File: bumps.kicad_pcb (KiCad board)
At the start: 2 copper layers, 111.1 x 65.4 mm, 126 parts, among them M1 CONN_1, M2 CONN_1, M3 CONN_1, P1 Micro-E, P10 Mot-A, P11 Mot-A, P12 Mot-X, P13 T1, P14 T2, P15 T3, P16 MPower, P17 PWM-2, P18 PWM-1, P19 END-X, P2 DIL6, P20 END-Y, P21 END-Z, P22 Mot-X, P23 Mot-Y, P24 Mot-Y, P25 Mot-Z, P26 Mot-Z, P27 Aux, P29 PWM, P3 Mot-E, P4 Mot-E, P5 DIL6, P6 DIL6, P7 DIL6, P8 P8 Header, P9 P9 Header, Q1 N-FET, Q2 N-FET, Q3 FDS9926A, Q4 FDS9926A, U1 E-Polo, U2 A-Polo, U3 X-Polo, U4 Y-Polo, U5 Z-Polo, U6 MC34063, U7 AP1117/3.3

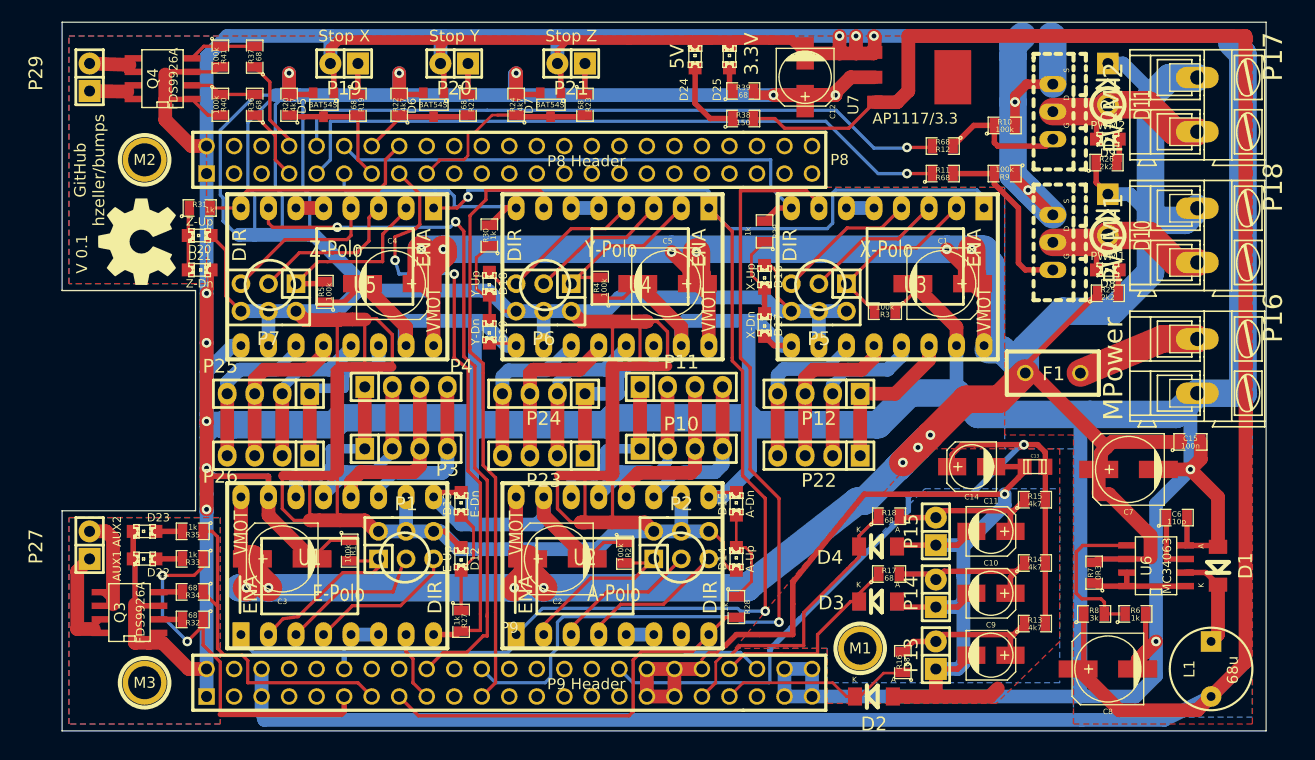
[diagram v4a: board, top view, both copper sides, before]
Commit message: o Some updates of labels.
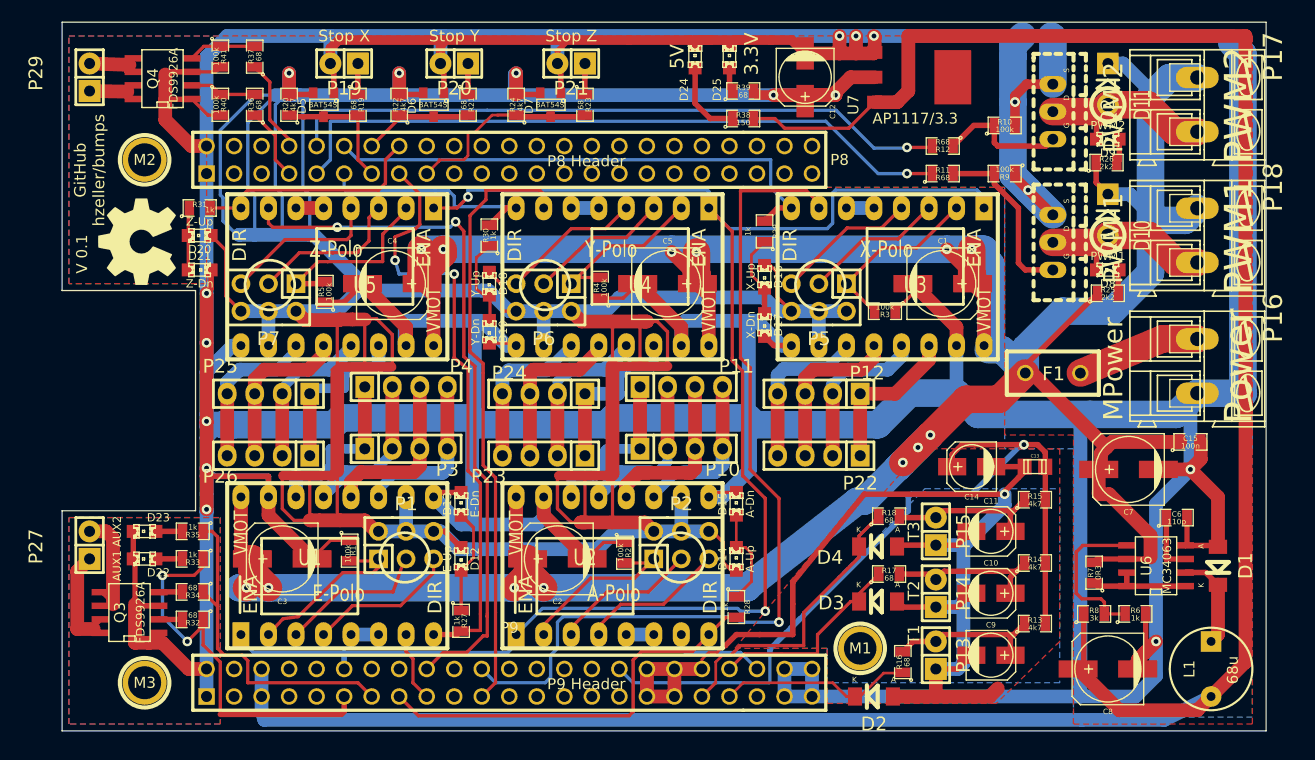
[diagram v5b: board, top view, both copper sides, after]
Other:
- board text added: "PWM1"
- board text added: "PWM2"
- board text added: "T1"
- board text added: "T2"
- board text added: "T3"
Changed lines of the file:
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@@
     (area 42.961076 19.039999 162.316583 94.234)
     (thickness 1.6)
-    (drawings 24)
+    (drawings 30)
     (tracks 1313)
     (zones 0)
@@
     (pad_to_mask_clearance 0)
     (aux_axis_origin 0 0)
-    (visible_elements FFFFFF7F)
+    (visible_elements FFFFEF7F)
     (pcbplotparams
       (layerselection 270565377)
@@
     (descr "1 pin")
     (tags "CONN DEV")
-    (fp_text reference P13 (at 0 -2.286 90) (layer F.SilkS)
+    (fp_text reference P13 (at 0 2.54 90) (layer F.SilkS)
       (effects (font (size 1.27 1.27) (thickness 0.2032)))
     )
@@
     (descr "1 pin")
     (tags "CONN DEV")
-    (fp_text reference P14 (at 0 -2.286 90) (layer F.SilkS)
+    (fp_text reference P14 (at 0 2.54 90) (layer F.SilkS)
       (effects (font (size 1.27 1.27) (thickness 0.2032)))
     )
@@
     (descr "1 pin")
     (tags "CONN DEV")
-    (fp_text reference P15 (at 0 -2.286 90) (layer F.SilkS)
+    (fp_text reference P15 (at 0 2.54 90) (layer F.SilkS)
       (effects (font (size 1.27 1.27) (thickness 0.2032)))
     )
@@
     (descr "1 pin")
     (tags "CONN DEV")
-    (fp_text reference P22 (at 0 -2.286 180) (layer F.SilkS)
+    (fp_text reference P22 (at -3.81 -2.54 180) (layer F.SilkS)
       (effects (font (size 1.27 1.27) (thickness 0.2032)))
     )
@@
     (descr "1 pin")
     (tags "CONN DEV")
-    (fp_text reference P23 (at 0 -2.286 180) (layer F.SilkS)
+    (fp_text reference P23 (at 5.08 -1.905 180) (layer F.SilkS)
       (effects (font (size 1.27 1.27) (thickness 0.2032)))
     )
@@
     (descr "1 pin")
     (tags "CONN DEV")
-    (fp_text reference P24 (at 0 -2.286 180) (layer F.SilkS)
+    (fp_text reference P24 (at 3.175 1.905 180) (layer F.SilkS)
       (effects (font (size 1.27 1.27) (thickness 0.2032)))
     )
@@
     (descr "1 pin")
     (tags "CONN DEV")
-    (fp_text reference P10 (at 0 -2.286) (layer F.SilkS)
+    (fp_text reference P10 (at 3.81 1.905) (layer F.SilkS)
       (effects (font (size 1.27 1.27) (thickness 0.2032)))
     )
@@
     (descr "1 pin")
     (tags "CONN DEV")
-    (fp_text reference P11 (at 0 -2.286) (layer F.SilkS)
+    (fp_text reference P11 (at 5.08 -1.905) (layer F.SilkS)
       (effects (font (size 1.27 1.27) (thickness 0.2032)))
     )
@@
     (descr "1 pin")
     (tags "CONN DEV")
-    (fp_text reference P12 (at 0 -2.286 180) (layer F.SilkS)
+    (fp_text reference P12 (at -4.445 1.905 180) (layer F.SilkS)
       (effects (font (size 1.27 1.27) (thickness 0.2032)))
     )
@@
       (xy -2.42316 3.59156)) (layer F.SilkS) (width 0.00254))
   )
+  (gr_text PWM2 (at 156.21 35.56 90) (layer F.SilkS)
+    (effects (font (size 2.54 2.54) (thickness 0.508)))
+  )
+  (gr_text PWM1 (at 156.21 47.625 90) (layer F.SilkS)
+    (effects (font (size 2.54 2.54) (thickness 0.508)))
+  )
+  (gr_text Power (at 156.21 59.69 90) (layer F.SilkS)
+    (effects (font (size 2.54 2.54) (thickness 0.508)))
+  )
+  (gr_text T2 (at 126.238 80.391 90) (layer F.SilkS)
+    (effects (font (size 1.0668 1.0668) (thickness 0.2032)))
+  )
+  (gr_text T1 (at 126.238 84.455 90) (layer F.SilkS)
+    (effects (font (size 1.0668 1.0668) (thickness 0.2032)))
+  )
+  (gr_text T3 (at 126.238 74.93 90) (layer F.SilkS)
+    (effects (font (size 1.0668 1.0668) (thickness 0.2032)))
+  )
   (gr_text "Stop Z" (at 94.615 29.21) (layer F.SilkS)

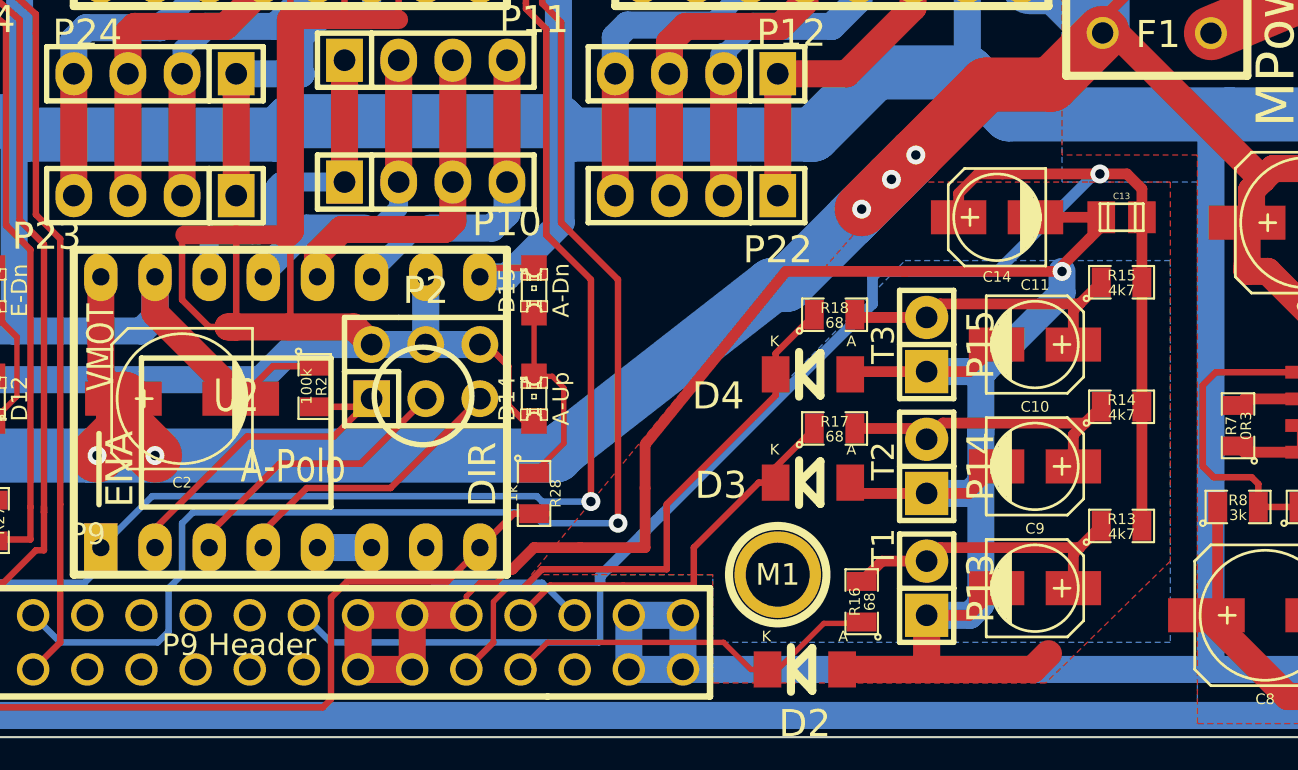
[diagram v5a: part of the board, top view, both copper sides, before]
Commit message: o Straighten out motor power trace to lower part a bit.
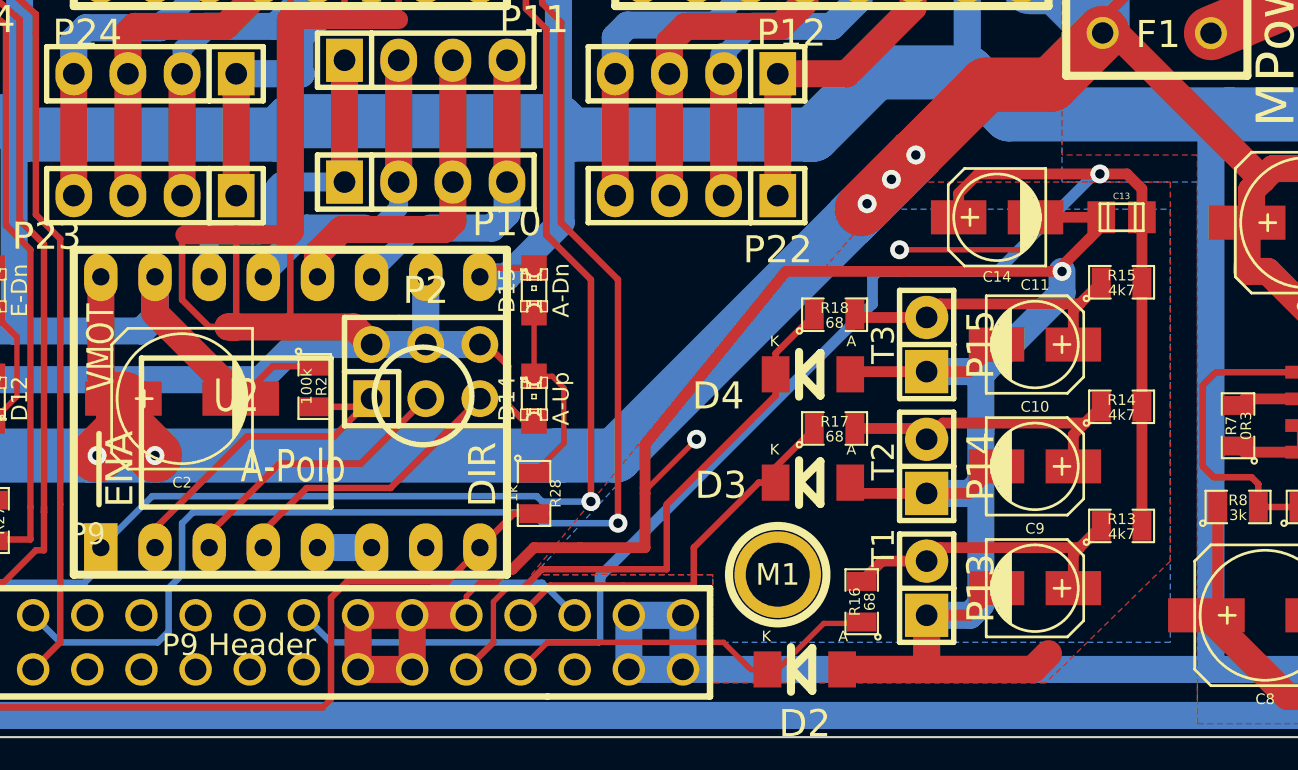
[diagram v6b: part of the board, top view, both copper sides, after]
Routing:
- net AGND: track 114.8 -> 125.8 mm, vias 1 -> 3
- net VMOT: track 322.8 -> 329.1 mm
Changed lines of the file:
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@@
     (thickness 1.6)
     (drawings 30)
-    (tracks 1313)
+    (tracks 1324)
     (zones 0)
     (modules 126)
@@
   )
   (setup
-    (last_trace_width 0.889)
+    (last_trace_width 0.254)
     (user_trace_width 0.3048)
     (user_trace_width 0.508)
@@
   (gr_line (start 158.75 27.94) (end 158.75 93.345) (angle 90) (layer Edge.Cuts) (width 0.1))
   (gr_line (start 47.625 27.94) (end 158.75 27.94) (angle 90) (layer Edge.Cuts) (width 0.1))
+  (segment (start 115.062 81.915) (end 115.062 81.788) (width 0.254) (layer F.Cu) (net 1))
+  (via (at 117.475 79.375) (size 0.889) (layers F.Cu B.Cu) (net 1))
+  (segment (start 115.062 81.788) (end 117.475 79.375) (width 0.254) (layer F.Cu) (net 1))
+  (segment (start 133.37286 68.961) (end 133.37286 69.82714) (width 0.254) (layer F.Cu) (net 1))
+  (via (at 127 70.485) (size 0.889) (layers F.Cu B.Cu) (net 1))
+  (segment (start 132.715 70.485) (end 127 70.485) (width 0.254) (layer F.Cu) (net 1))
+  (segment (start 133.37286 69.82714) (end 132.715 70.485) (width 0.254) (layer F.Cu) (net 1))
   (segment (start 128.27 87.63) (end 130.27914 87.63) (width 0.508) (layer F.Cu) (net 1))
   (segment (start 130.27914 87.63) (end 131.54914 86.36) (width 0.508) (layer F.Cu) (net 1))
@@
   (segment (start 106.68 86.741) (end 107.315 86.106) (width 0.254) (layer F.Cu) (net 1))
   (segment (start 108.712 85.471) (end 108.839 85.471) (width 0.508) (layer F.Cu) (net 1))
-  (segment (start 115.062 84.455) (end 115.062 81.661) (width 0.508) (layer F.Cu) (net 1))
+  (segment (start 115.062 84.455) (end 115.062 81.915) (width 0.508) (layer F.Cu) (net 1))
+  (segment (start 115.062 81.915) (end 115.062 81.661) (width 0.508) (layer F.Cu) (net 1))
   (segment (start 115.062 79.629) (end 121.666 71.501) (width 0.508) (layer F.Cu) (net 1))
   (segment (start 133.37286 68.961) (end 136.4615 68.961) (width 0.508) (layer F.Cu) (net 1))
@@
   (segment (start 113.284 85.471) (end 116.078 85.471) (width 0.3048) (layer F.Cu) (net 154))
   (segment (start 121.18594 77.31506) (end 121.18594 76.327) (width 0.3048) (layer F.Cu) (net 154))
+  (segment (start 64.135 54.61) (end 66.675 54.61) (width 1.27) (layer B.Cu) (net 155))
   (segment (start 118.999 34.671) (end 116.75364 34.671) (width 1.27) (layer F.Cu) (net 155))
   (segment (start 116.75364 34.671) (end 116.205 35.21964) (width 1.27) (layer F.Cu) (net 155))
@@
   (segment (start 112.395 53.34) (end 113.665 54.61) (width 1.27) (layer B.Cu) (net 155))
   (segment (start 113.665 54.61) (end 114.935 54.61) (width 1.27) (layer B.Cu) (net 155))
-  (segment (start 64.135 54.61) (end 66.675 54.61) (width 1.27) (layer B.Cu) (net 155))
   (segment (start 66.675 54.61) (end 69.215 54.61) (width 1.27) (layer B.Cu) (net 155))
   (segment (start 69.215 54.61) (end 73.025 54.61) (width 1.27) (layer B.Cu) (net 155))
@@
   (segment (start 100.33 88.9) (end 112.903 88.9) (width 0.3048) (layer B.Cu) (net 157))
   (segment (start 99.06 87.63) (end 99.06 87.757) (width 0.254) (layer B.Cu) (net 157))
+  (via (at 125.476 68.326) (size 0.889) (layers F.Cu B.Cu) (net 158))
+  (segment (start 125.476 68.326) (end 124.714 69.088) (width 2.54) (layer B.Cu) (net 158))
+  (via (at 126.619 67.183) (size 0.889) (layers F.Cu B.Cu) (net 158))
+  (via (at 127.762 66.04) (size 0.889) (layers F.Cu B.Cu) (net 158))
+  (segment (start 127.762 66.04) (end 127.6985 66.1035) (width 2.54) (layer B.Cu) (net 158))
+  (segment (start 127.6985 66.1035) (end 127.762 66.04) (width 2.54) (layer B.Cu) (net 158))
+  (segment (start 111.125 80.137) (end 113.665 80.137) (width 2.54) (layer B.Cu) (net 158))
+  (segment (start 126.619 67.183) (end 127.762 66.04) (width 2.54) (layer B.Cu) (net 158))
+  (segment (start 124.714 69.088) (end 126.619 67.183) (width 2.54) (layer B.Cu) (net 158))
+  (segment (start 124.714 69.088) (end 125.222 68.58) (width 2.54) (layer B.Cu) (net 158))
+  (segment (start 113.665 80.137) (end 127.762 66.04) (width 2.54) (layer B.Cu) (net 158))
   (segment (start 143.1925 52.959) (end 136.525 59.6265) (width 0.508) (layer F.Cu) (net 158))
   (segment (start 136.525 59.6265) (end 136.525 60.31484) (width 0.508) (layer F.Cu) (net 158))
@@
   (via (at 89.357202 80.137) (size 0.889) (layers F.Cu B.Cu) (net 158))
   (segment (start 89.357202 80.137) (end 89.027 80.137) (width 2.54) (layer B.Cu) (net 158))
-  (segment (start 111.252 79.756) (end 110.871 80.137) (width 2.54) (layer B.Cu) (net 158))
-  (segment (start 124.714 69.088) (end 121.666 72.136) (width 2.54) (layer B.Cu) (net 158))
-  (segment (start 121.031 72.136) (end 121.666 72.136) (width 2.54) (layer B.Cu) (net 158))
-  (segment (start 111.252 79.756) (end 121.031 72.136) (width 2.54) (layer B.Cu) (net 158))
-  (segment (start 110.871 80.137) (end 92.075 80.137) (width 2.54) (layer B.Cu) (net 158))
+  (segment (start 110.871 80.137) (end 111.125 80.137) (width 2.54) (layer B.Cu) (net 158))
+  (segment (start 111.125 80.137) (end 92.075 80.137) (width 2.54) (layer B.Cu) (net 158))
   (segment (start 92.075 80.137) (end 89.027 80.137) (width 2.54) (layer B.Cu) (net 158))
   (segment (start 132.715 57.785) (end 133.35 57.15) (width 1.27) (layer B.Cu) (net 158))
@@
   (segment (start 133.35 50.292) (end 131.953 48.895) (width 2.54) (layer B.Cu) (net 158))
   (segment (start 133.35 57.15) (end 133.35 50.292) (width 2.54) (layer B.Cu) (net 158))
-  (via (at 126.619 67.183) (size 0.889) (layers F.Cu B.Cu) (net 158))
-  (via (at 127.762 66.04) (size 0.889) (layers F.Cu B.Cu) (net 158))
   (segment (start 136.525 60.31484) (end 134.10184 62.738) (width 2.54) (layer F.Cu) (net 158))
-  (segment (start 125.222 68.58) (end 124.714 69.088) (width 2.54) (layer B.Cu) (net 158))
-  (via (at 125.222 68.58) (size 0.889) (layers F.Cu B.Cu) (net 158))
   (segment (start 131.064 62.738) (end 127.762 66.04) (width 2.54) (layer F.Cu) (net 158))
   (segment (start 127.762 66.04) (end 126.619 67.183) (width 2.54) (layer F.Cu) (net 158))
-  (segment (start 126.619 67.183) (end 125.222 68.58) (width 2.54) (layer F.Cu) (net 158))
+  (segment (start 126.619 67.183) (end 125.476 68.326) (width 2.54) (layer F.Cu) (net 158))
+  (segment (start 125.476 68.326) (end 125.222 68.58) (width 2.54) (layer F.Cu) (net 158))
   (segment (start 134.10184 62.738) (end 131.064 62.738) (width 2.54) (layer F.Cu) (net 158))
   (segment (start 132.715 57.785) (end 133.096 58.166) (width 1.27) (layer B.Cu) (net 158))
   (segment (start 134.37616 58.166) (end 136.525 60.31484) (width 2.54) (layer B.Cu) (net 158))
   (segment (start 133.096 58.166) (end 134.37616 58.166) (width 2.54) (layer B.Cu) (net 158))
-  (segment (start 124.714 69.088) (end 126.619 67.183) (width 2.54) (layer B.Cu) (net 158))
-  (segment (start 126.619 67.183) (end 127.762 66.04) (width 2.54) (layer B.Cu) (net 158))
   (segment (start 80.85582 52.07) (end 80.85582 51.26482) (width 1.27) (layer F.Cu) (net 158))
   (segment (start 80.85582 51.26482) (end 82.804 49.31664) (width 2.54) (layer F.Cu) (net 158))
@@
     (polygon
       (pts
-        (xy 139.7 88.9) (xy 118.237 88.9) (xy 118.237 85.725) (xy 112.776 85.725) (xy 127.254 70.993)
-        (xy 139.7 70.993)
+        (xy 139.7 88.9) (xy 118.237 88.9) (xy 118.237 85.725) (xy 109.855 85.725) (xy 125.73 68.58)
+        (xy 139.7 68.58)
       )
     )
